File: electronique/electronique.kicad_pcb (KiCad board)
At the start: 2 copper layers, 70 x 50 mm, 51 parts, among them J1 Conn_01x02, J10 PHOTOD3, J11 PHOTOD4, J12 Ultrason 3, J13 Moteur 1, J14 Moteur 2, J2 Conn_02x07_Odd_Even, J3 Camera, J4 TOF1, J5 Conn_01x06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

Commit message: Moins de vias.
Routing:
- net GND: track 109.9 -> 105.1 mm, vias 18 -> 13

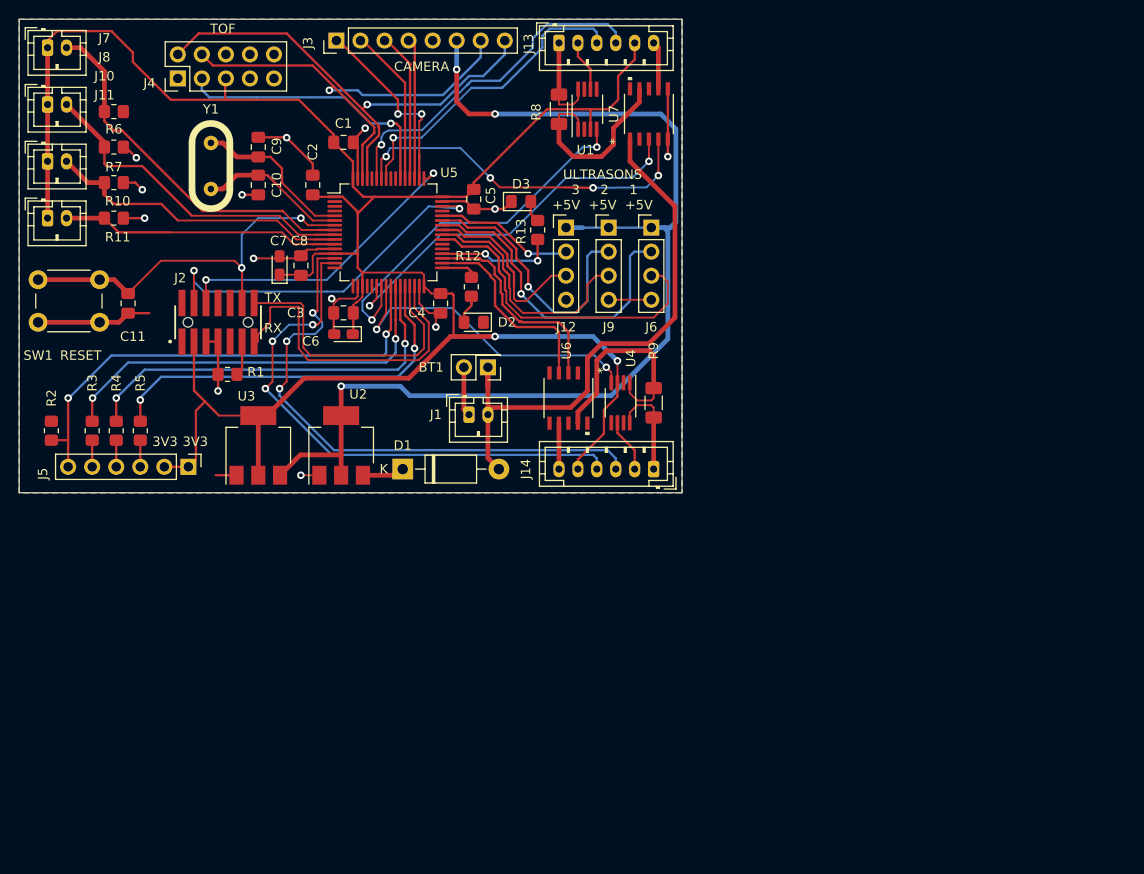
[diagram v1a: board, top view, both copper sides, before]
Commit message: ajout de vias
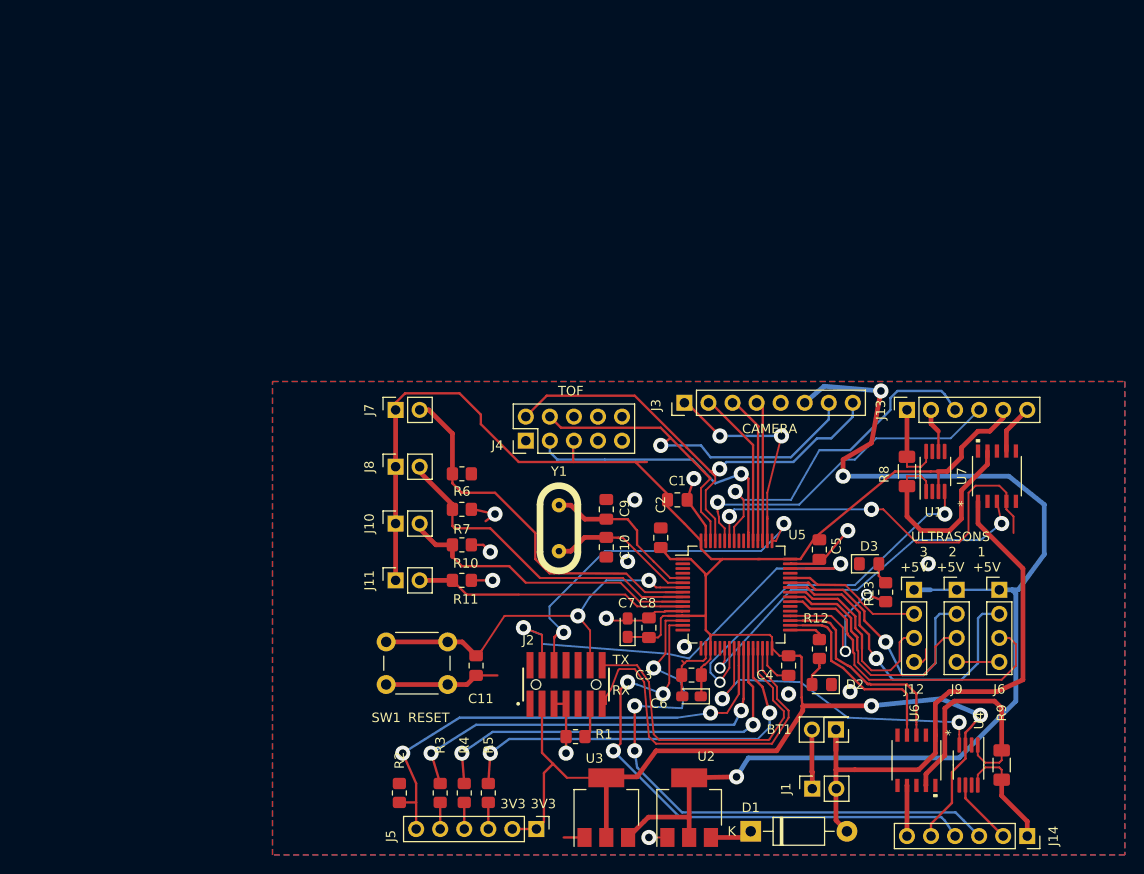
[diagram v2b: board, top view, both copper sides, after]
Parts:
- J1, J10, J11, J7, J8: footprint Connector_JST:JST_PH_B2B-PH-K_1x02_P2.00mm_Vertical -> Connector_PinSocket_2.54mm:PinSocket_1x02_P2.54mm_Vertical
- J13, J14: footprint Connector_JST:JST_PH_B6B-PH-K_1x06_P2.00mm_Vertical -> Connector_PinSocket_2.54mm:PinSocket_1x06_P2.54mm_Vertical
- moved J14 55.3 mm to (118.5, 98.2), turned to 270 degrees
- moved J1 53.6 mm to (95.8, 93.2), turned to 90 degrees
- moved J13 53.4 mm to (105.8, 53.2), turned to 90 degrees
- moved BT1 53.0 mm to (98.2, 87.0)
- moved C10 53.0 mm to (74.0, 67.8)
- moved C11 53.0 mm to (60.2, 80.2)
- moved C3 53.0 mm to (83.0, 81.2)
- moved C4 53.0 mm to (93.2, 80.2)
- moved C6 53.0 mm to (83.0, 83.5)
- moved C7 53.0 mm to (76.2, 76.2)
- moved C8 53.0 mm to (78.5, 76.2)
- moved C9 53.0 mm to (74.0, 63.8)
- moved D1 53.0 mm to (89.2, 97.8)
- moved D2 53.0 mm to (96.8, 82.2)
- moved D3 53.0 mm to (101.8, 69.5)
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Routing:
- net GND: track 105.1 -> 92.9 mm, vias 13 -> 14
- net /SWDIO: track 39.0 -> 49.6 mm
- net +5V: track 119.5 -> 127.1 mm
- net /SWCLK: track 32.4 -> 38.6 mm
- net +3V3: track 238.7 -> 244.8 mm
- net /M1N_PWM: track 38.1 -> 43.8 mm, vias 4 -> 2
- net /AXELED: track 12.6 -> 17.8 mm
- net /TX1: track 30.4 -> 35.1 mm
- net /M2_A: track 59.6 -> 64.1 mm
- net /RX1: track 34.1 -> 38.5 mm
- net /M1_A: track 32.9 -> 36.9 mm
- net /SDA: track 47.6 -> 50.4 mm
- net /CS: track 20.7 -> 23.3 mm
- net /RSP1: track 20.3 -> 22.8 mm
- net /RSP2: track 22.7 -> 25.1 mm
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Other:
- board outline removed

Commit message: Mise a jour CI
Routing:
- net /M1N_PWM: track 43.8 -> 40.1 mm
- net GND: track 92.9 -> 90.7 mm
- net +3V3: track 244.8 -> 243.6 mm

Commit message: Circuit imprimé FINAL.
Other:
- board outline added: 90 x 50 mm
